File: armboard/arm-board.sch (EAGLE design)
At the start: 34 parts

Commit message: swapped led_xb_tx package
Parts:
- LED_XB_TX: device SparkFun-LED:LED-GREEN1206-BOTTOM -> SparkFun-LED:LED-GREEN1206
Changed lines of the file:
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@@
 <part name="GND3" library="SparkFun-Aesthetics" deviceset="GND" device=""/>
 <part name="LED_XB_RX" library="SparkFun-LED" deviceset="LED" device="1206" value="RED"/>
-<part name="LED_XB_TX" library="SparkFun-LED" deviceset="LED-GREEN" device="1206-BOTTOM" value="GREEN"/>
+<part name="LED_XB_TX" library="SparkFun-LED" deviceset="LED-GREEN" device="1206" value="GREEN"/>
 <part name="R2" library="SparkFun-Passives" deviceset="RESISTOR" device="1206" value="1k"/>
 <part name="R3" library="SparkFun-Passives" deviceset="RESISTOR" device="1206" value="1k"/>

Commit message: played with placement a bit
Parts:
- renumbered EE to FET_EE
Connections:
- removed net FROM_EE_GND: FET_EEG$2.D
- removed net GATE_PWR_EE: FET_EEG$2.G
- net +3V3: no longer R1.2
- net +5V: now also R1.2
- net EEPWR_GND: now also FET_EEG$2.D
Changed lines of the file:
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@@
 <part name="GND2" library="SparkFun" deviceset="GND" device=""/>
 <part name="GND8" library="SparkFun-Aesthetics" deviceset="GND" device=""/>
-<part name="EE" library="transistor-power" deviceset="IRF7910PBF" device=""/>
+<part name="FET_EE" library="transistor-power" deviceset="IRF7910PBF" device=""/>
 <part name="GND9" library="SparkFun-Aesthetics" deviceset="GND" device=""/>
 <part name="GND11" library="SparkFun-Aesthetics" deviceset="GND" device=""/>
@@
 <part name="GND13" library="SparkFun-Aesthetics" deviceset="GND" device=""/>
 <part name="P+4" library="supply1" deviceset="+12V" device=""/>
-<part name="+3V2" library="supply1" deviceset="+3V3" device=""/>
 <part name="+3V3" library="supply1" deviceset="+3V3" device=""/>
 <part name="+3V4" library="supply1" deviceset="+3V3" device=""/>
@@
 <part name="ENC_J2" library="con-molex" deviceset="53?-03" device="047"/>
 <part name="ENC_J3" library="con-molex" deviceset="53?-03" device="047"/>
+<part name="P+13" library="supply1" deviceset="+5V" device=""/>
 </parts>
 <sheets>
@@
 <instance part="GND13" gate="1" x="15.24" y="58.42"/>
 <instance part="P+4" gate="1" x="22.86" y="48.26"/>
-<instance part="+3V2" gate="G$1" x="10.16" y="48.26"/>
+<instance part="P+13" gate="1" x="10.16" y="48.26"/>
 </instances>
 <busses>
@@
 <wire x1="10.16" y1="66.04" x2="10.16" y2="71.12" width="0.1524" layer="91"/>
 </segment>
+<segment>
+<pinref part="R1" gate="G$1" pin="2"/>
+<pinref part="P+13" gate="1" pin="+5V"/>
+<wire x1="10.16" y1="43.18" x2="10.16" y2="45.72" width="0.1524" layer="91"/>
+</segment>
 </net>
 <net name="GND" class="0">
@@
 <pinref part="R1" gate="G$1" pin="1"/>
 <pinref part="LED_PWR" gate="G$1" pin="A"/>
-</segment>
-</net>
-<net name="+3V3" class="0">
-<segment>
-<wire x1="10.16" y1="45.72" x2="10.16" y2="43.18" width="0.1524" layer="91"/>
-<pinref part="R1" gate="G$1" pin="2"/>
 </segment>
 </net>
@@
 </plain>
 <instances>
-<instance part="EE" gate="G$1" x="20.32" y="35.56"/>
-<instance part="EE" gate="G$2" x="66.04" y="35.56"/>
+<instance part="FET_EE" gate="G$1" x="20.32" y="35.56"/>
+<instance part="FET_EE" gate="G$2" x="66.04" y="35.56"/>
 <instance part="GND9" gate="1" x="22.86" y="25.4"/>
 <instance part="GND11" gate="1" x="68.58" y="25.4"/>
@@
 </busses>
 <nets>
-<net name="FROM_EE_GND" class="0">
-<segment>
-<pinref part="EE" gate="G$2" pin="D"/>
-<wire x1="68.58" y1="40.64" x2="68.58" y2="43.18" width="0.1524" layer="91"/>
-</segment>
-</net>
 <net name="GND" class="0">
 <segment>
-<pinref part="EE" gate="G$1" pin="S"/>
+<pinref part="FET_EE" gate="G$1" pin="S"/>
 <pinref part="GND9" gate="1" pin="GND"/>
 <wire x1="22.86" y1="30.48" x2="22.86" y2="27.94" width="0.1524" layer="91"/>
 </segment>
 <segment>
-<pinref part="EE" gate="G$2" pin="S"/>
+<pinref part="FET_EE" gate="G$2" pin="S"/>
 <wire x1="68.58" y1="30.48" x2="68.58" y2="27.94" width="0.1524" layer="91"/>
 <pinref part="GND11" gate="1" pin="GND"/>
@@
 <net name="GATE_PWR_SOL" class="0">
 <segment>
-<pinref part="EE" gate="G$1" pin="G"/>
+<pinref part="FET_EE" gate="G$1" pin="G"/>
 <wire x1="17.78" y1="33.02" x2="15.24" y2="33.02" width="0.1524" layer="91"/>
 <label x="15.24" y="33.02" size="1.016" layer="95" rot="R180" xref="yes"/>
-</segment>
-</net>
-<net name="GATE_PWR_EE" class="0">
-<segment>
-<pinref part="EE" gate="G$2" pin="G"/>
-<wire x1="63.5" y1="33.02" x2="60.96" y2="33.02" width="0.1524" layer="91"/>
-<label x="60.96" y="33.02" size="1.016" layer="95" rot="R180" xref="yes"/>
 </segment>
 </net>
@@
 <pinref part="CON_PWR_SOL" gate="G$1" pin="GND"/>
 <wire x1="25.4" y1="55.88" x2="22.86" y2="55.88" width="0.1524" layer="91"/>
-<pinref part="EE" gate="G$1" pin="D"/>
+<pinref part="FET_EE" gate="G$1" pin="D"/>
 <wire x1="22.86" y1="55.88" x2="22.86" y2="40.64" width="0.1524" layer="91"/>
 </segment>
@@
 <net name="EEPWR_GND" class="0">
 <segment>
+<pinref part="FET_EE" gate="G$2" pin="D"/>
+<wire x1="68.58" y1="40.64" x2="68.58" y2="55.88" width="0.1524" layer="91"/>
 <pinref part="CON_PWR_EE" gate="G$1" pin="GND"/>
-<wire x1="71.12" y1="55.88" x2="68.58" y2="55.88" width="0.1524" layer="91"/>
-<wire x1="68.58" y1="55.88" x2="68.58" y2="43.18" width="0.1524" layer="91"/>
+<wire x1="68.58" y1="55.88" x2="71.12" y2="55.88" width="0.1524" layer="91"/>
 </segment>
 </net>
@@
 </schematic>
 </drawing>
+<compatibility>
+<note version="6.3" minversion="6.2.2" severity="warning">
+Since Version 6.2.2 text objects can contain more than one line,
+which will not be processed correctly with this version.
+</note>
+</compatibility>
 </eagle>

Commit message: finished most of the arm board, excl encoders
waiting on clarification on timer ccp pins before connecting encoders
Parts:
- removed C3: 330uF, SparkFun-Capacitors:CAP_POLE
- removed D9: SMAJ5920, SparkFun-DiscreteSemi:DIODE-SCHOTTKY-MBRA140
- removed DYNAFET2, DYNAFET3: IRF7910PBF, transistor-power:IRF7910PBF
- removed X4: (no value), con-subd:F15V
- added C1: (no value), SparkFun-Capacitors:100UF-25V-20%(PTH)
- added C10, C11, C7, C8, C9: 0.1uF, SparkFun-Capacitors:CAP1206
- added H1, H2: MOUNT-HOLE3.2, holes:MOUNT-HOLE3.2
- added R5, R6, R7, R8, R9: 1k, SparkFun-Resistors:RESISTOR1206
- added U$2: IRF7910PBF, transistor-power:IRF7910PBF
- added U$4: MAX3232, MRDT-LIB2014:MAX3232
- added X1: 53047-06, con-molex:53047-06
- renumbered ENC_J3 to ENC_EI, ENC_J4 to ENC_EO, ENC_J5 to ENC_WI, ENC_J6 to ENC_WO
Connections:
- net EEPWR_GND renamed EE_GND
- net ENC_J3 renamed ENC_EI
- net ENC_J4 renamed ENC_EO
- net ENC_J5 renamed ENC_WI
- net ENC_J6 renamed ENC_WO
- net N$5 renamed DYNA1_GND
- removed net N$6: DYNA2.1, DYNAFET2G$2.D
- removed net N$7: DYNA3.1, DYNAFET3G$2.D
- new net DYNA2_GND: DYNA2.1, U$2G$1.D
- new net DYNA3_GND: DYNA3.1, U$2G$2.D
- new net GATE_PWR_EE: FET_EEG$2.G, R6.2, U$1.PH1
- new net N$15: C7.2, U$4.C1-
- new net N$16: C7.1, U$4.C1+
- new net N$17: C8.1, U$4.C2+
- new net N$18: C8.2, U$4.C2-
- new net N$19: C10.1, U$4.V-
- new net N$20: C9.1, U$4.V+
- new net R_OUT1: U$4.R_OUT1, X1-2.S
- new net T_OUT1: U$4.T_OUT1, X1-1.S
- new net VCC1: C11.1, U$4.VCC
- net +12V: now also C1.+; no longer C3.+
- net DYNA_RX: now also U$1.PC6
- net DYNA_SWD: no longer D9.C
- net DYNA_TX: now also U$1.PC7
- net GATE_DYNA1: now also R7.2, U$1.PE2
- net GATE_DYNA2: now also R8.2, U$1.PE3, U$2G$1.G; no longer DYNAFET2G$2.G
- net GATE_DYNA3: now also R9.2, U$1.PD7, U$2G$2.G; no longer DYNAFET3G$2.G
- net GATE_PWR_SOL: now also R5.2, U$1.PH0
- net GND: now also C1.-, C10.2, C11.2, C9.2, R5.1, R6.1, R7.1, R8.1, R9.1, U$2G$1.S, U$2G$2.S, U$4.GND, X1-4.S; no longer C3.-, D9.A, DYNAFET2G$2.S, DYNAFET3G$2.S, X4.13, X4.5
- net J2_RC1: now also U$1.PK5, X1-3.S; no longer X4.4
- net J2_RS232RX: now also U$1.PK0, U$4.R_IN1; no longer X4.3
- net J2_RS232TX: now also U$1.PK1, U$4.T_IN1; no longer X4.2
- net J2_TTLRX: now also U$1.PA4, X1-6.S; no longer X4.7
- net J2_TTLTX: now also U$1.PA5, X1-5.S; no longer X4.6
- net TRI_EN: now also U$1.PB2
- net XB_RX: now also U$1.PQ3/PA2
- net XB_TX: now also U$1.PQ2/PA3

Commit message: swapped mlx-3-pin for mlx-2x3-pin
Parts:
- removed CON_PWR_EE, CON_PWR_J2, CON_PWR_MAIN, CON_PWR_SOL: MLX-3-PIN, MRDT-2015-General:MLX-3-PIN
- removed D8: SMAJ5920, SparkFun-DiscreteSemi:DIODE-SCHOTTKY-MBRA140
- removed DYNAFET1, FET_EE, U$2: IRF7910PBF, transistor-power:IRF7910PBF
- removed X1: 53047-06, con-molex:53047-06
- added CON_PWR_MAIN_J2, CON_PWR_SOL_EE: MLX-2X3-PIN, MRDT-2015-General:MLX-2X3-PIN
- added CTRL_J2: 53047-06, con-molex:53047-06
- added D1: SMAJ5920, SparkFun-DiscreteSemi:DIODE-SCHOTTKY-MBRA140
- added FET_EE1: IRF7910PBF, transistor-power:IRF7910PBF
- added R10, R11, R12, R13, R14: 5k, SparkFun-Resistors:RESISTOR1206
- R5, R6, R7, R8, R9: value 1k -> 5k
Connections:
- removed net DYNA2_GND: DYNA2.1, U$2G$1.D
- removed net DYNA3_GND: DYNA3.1, U$2G$2.D
- removed net EE_GND: CON_PWR_EE.GND, FET_EEG$2.D
- removed net SOL_GND: CON_PWR_SOL.GND, FET_EEG$1.D
- new net DYNA1_GND1: DYNA2.1
- new net DYNA1_GND2: DYNA3.1
- new net EE_GND1: CON_PWR_SOL_EE.GND_2, FET_EE1G$1.D
- new net N$10: R8.2, R9.1
- new net N$11: FET_EE1G$1.G, R12.1, R6.2
- new net N$12: R13.2, R14.1
- new net N$5: CON_PWR_SOL_EE.12V_2
- new net N$6: R11.1, R7.2
- new net N$7: FET_EE1G$2.G, R10.2, R5.1
- new net SOL_GND1: CON_PWR_SOL_EE.GND_1, FET_EE1G$2.D
- net +12V: now also CON_PWR_MAIN_J2.12V_1, CON_PWR_MAIN_J2.12V_2, CON_PWR_SOL_EE.12V_1; no longer CON_PWR_EE.12V, CON_PWR_J2.12V, CON_PWR_MAIN.12V, CON_PWR_SOL.12V
- net +5V: now also CON_PWR_MAIN_J2.5V_1; no longer CON_PWR_MAIN.5V
- net DYNA1_GND: no longer DYNAFET1G$2.D
- net DYNA_SWD: now also D1.C; no longer D8.C
- net GATE_DYNA1: now also R11.2; no longer DYNAFET1G$2.G, R7.2
- net GATE_DYNA2: now also R9.2; no longer R8.2, U$2G$1.G
- net GATE_DYNA3: now also R14.2; no longer R9.2, U$2G$2.G
- net GATE_PWR_EE: now also R12.2, U$1.PH0; no longer FET_EEG$2.G, R6.2, U$1.PH1
- net GATE_PWR_SOL: now also U$1.PH1; no longer FET_EEG$1.G, U$1.PH0
- net GND: now also CON_PWR_MAIN_J2.GND_1, CON_PWR_MAIN_J2.GND_2, CTRL_J2-4.S, D1.A, FET_EE1G$1.S, FET_EE1G$2.S, R10.1, R13.1; no longer CON_PWR_J2.GND, CON_PWR_MAIN.GND, D8.A, DYNAFET1G$2.S, FET_EEG$1.S, FET_EEG$2.S, R5.1, R9.1, U$2G$1.S, U$2G$2.S, X1-4.S
- net J2_RC1: now also CTRL_J2-3.S; no longer X1-3.S
- net J2_TTLRX: now also CTRL_J2-6.S; no longer X1-6.S
- net J2_TTLTX: now also CTRL_J2-5.S; no longer X1-5.S
- net R_OUT1: now also CTRL_J2-2.S; no longer X1-2.S
- net T_OUT1: now also CTRL_J2-1.S; no longer X1-1.S
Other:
- note added: "DECOUPLING CAP"
- note added: "DYNA DATA TX/RX INDICATOR"
- note added: "POWER INDICATOR"
- note added: "PWR_EE"
- note added: "PWR_J2"
- note added: "PWR_MAIN"
- note added: "PWR_SOL"

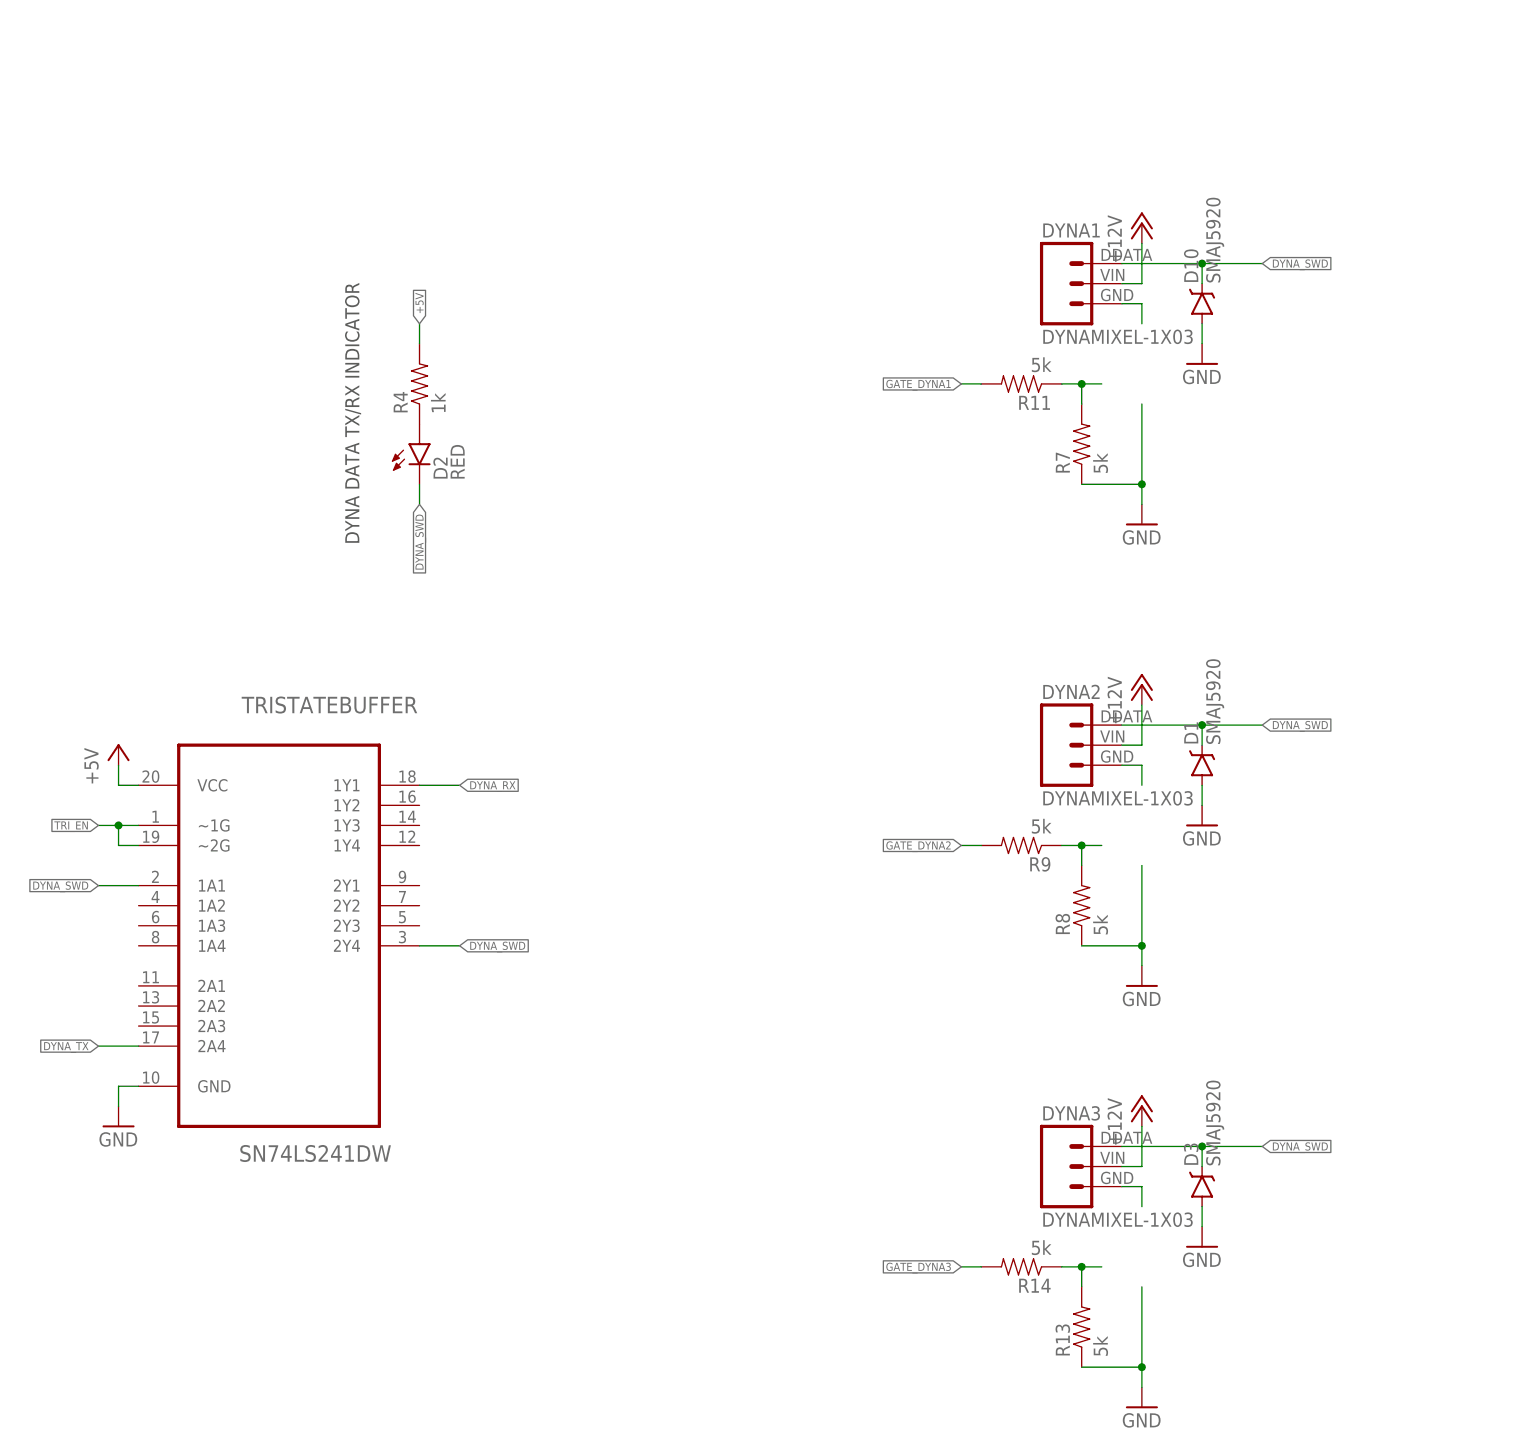
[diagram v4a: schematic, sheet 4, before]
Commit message: changing switch fets, rearranging board
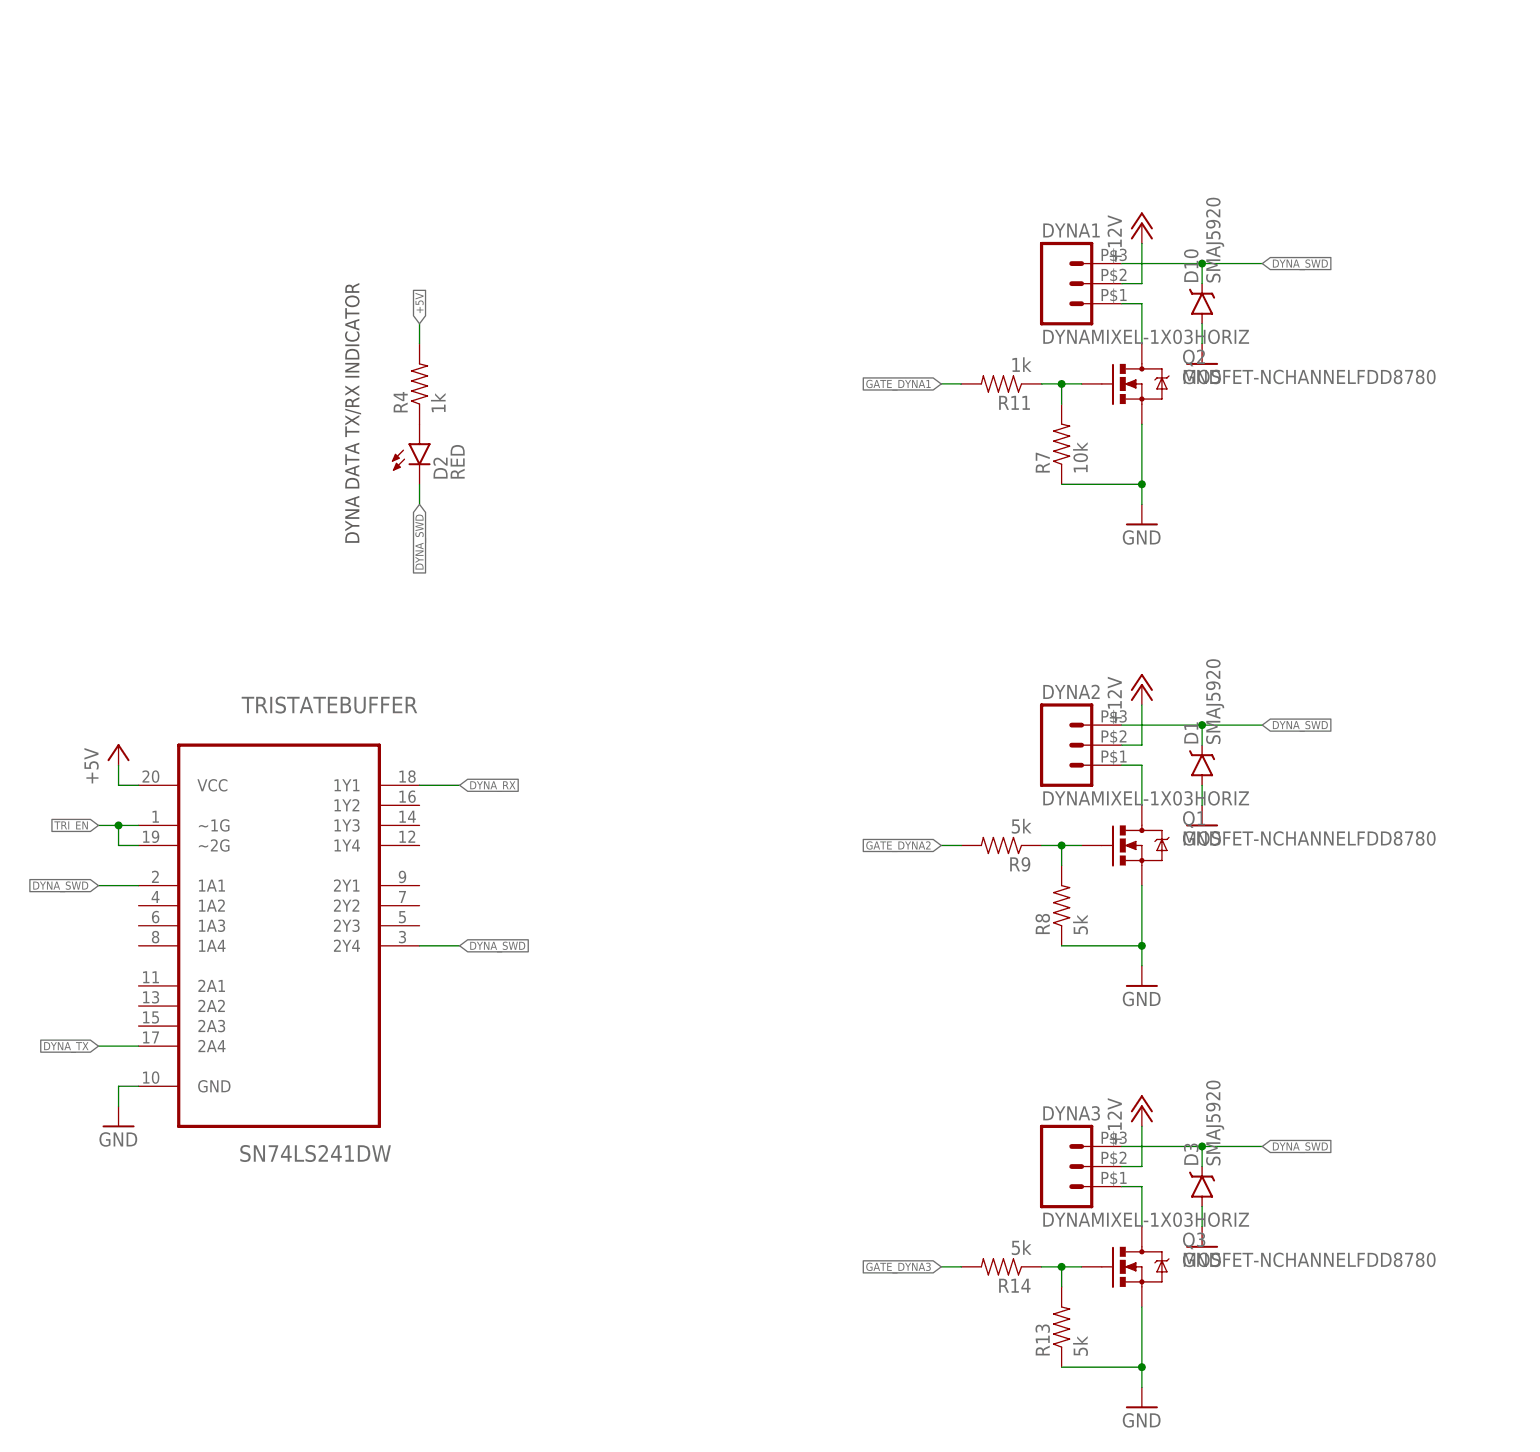
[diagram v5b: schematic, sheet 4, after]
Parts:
- added Q1, Q2, Q3: MOSFET-NCHANNELFDD8780, SparkFun-DiscreteSemi:MOSFET-NCHANNELFDD8780
- DYNA1, DYNA2, DYNA3: value DYNAMIXEL-1X03 -> DYNAMIXEL-1X03HORIZ; device MRDT-2015-Arm:DYNAMIXEL-1X03 -> MRDT-2015-Arm:DYNAMIXEL-1X03HORIZ
- R11: value 5k -> 1k
- R7: value 5k -> 10k
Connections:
- net DYNA1_GND: now also Q2.D
- net DYNA1_GND1: now also Q1.D
- net DYNA1_GND2: now also Q3.D
- net GND: now also Q1.S, Q3.S
- net N$10: now also Q1.G
- net N$12: now also Q3.G
- net N$6: now also Q2.G
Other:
- moved on the sheet: DYNA1, DYNA2, DYNA3, R11, R13, R14, R7, R8, R9
